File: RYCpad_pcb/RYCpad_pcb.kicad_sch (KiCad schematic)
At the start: 61 parts, among them J1 USB_C_Receptacle_USB2.0, J2 AVR ISP, K1 KEYSW, K10 KEYSW, K11 KEYSW, K12 KEYSW, K13 KEYSW, K14 KEYSW, K15 KEYSW, K16 KEYSW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

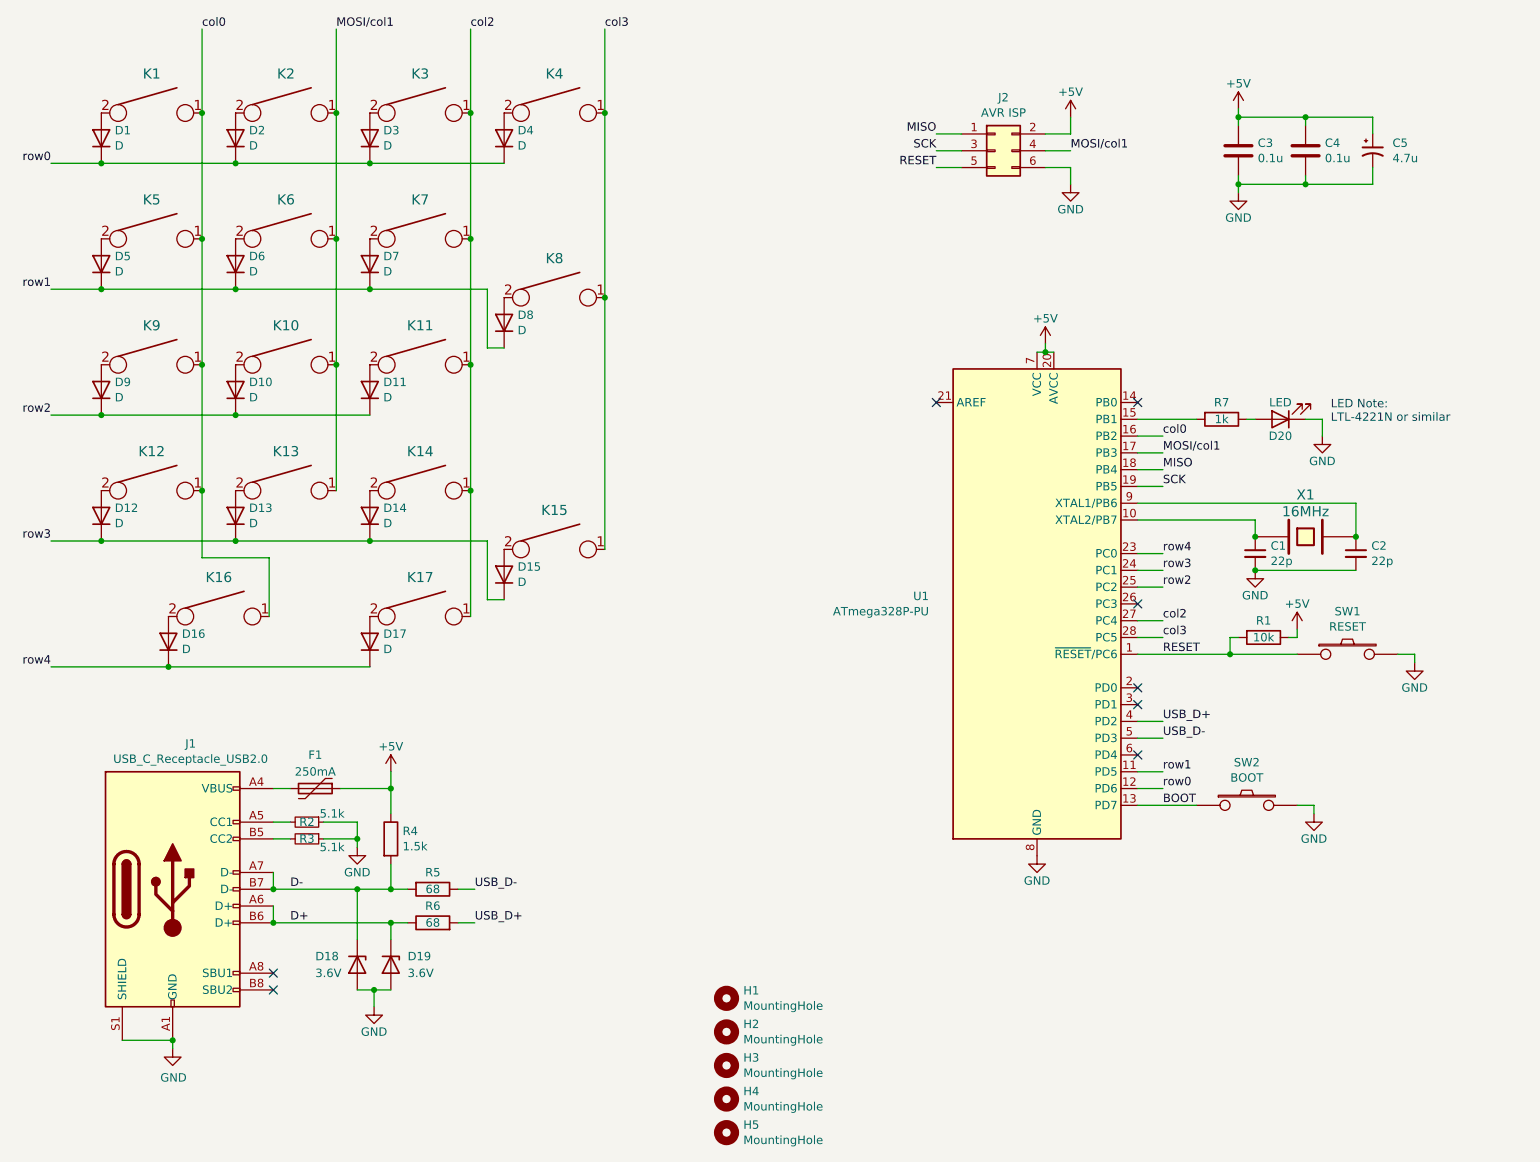
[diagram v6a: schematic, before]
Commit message: adjust col1 pin
change col1 pin PB3 >>> PC3
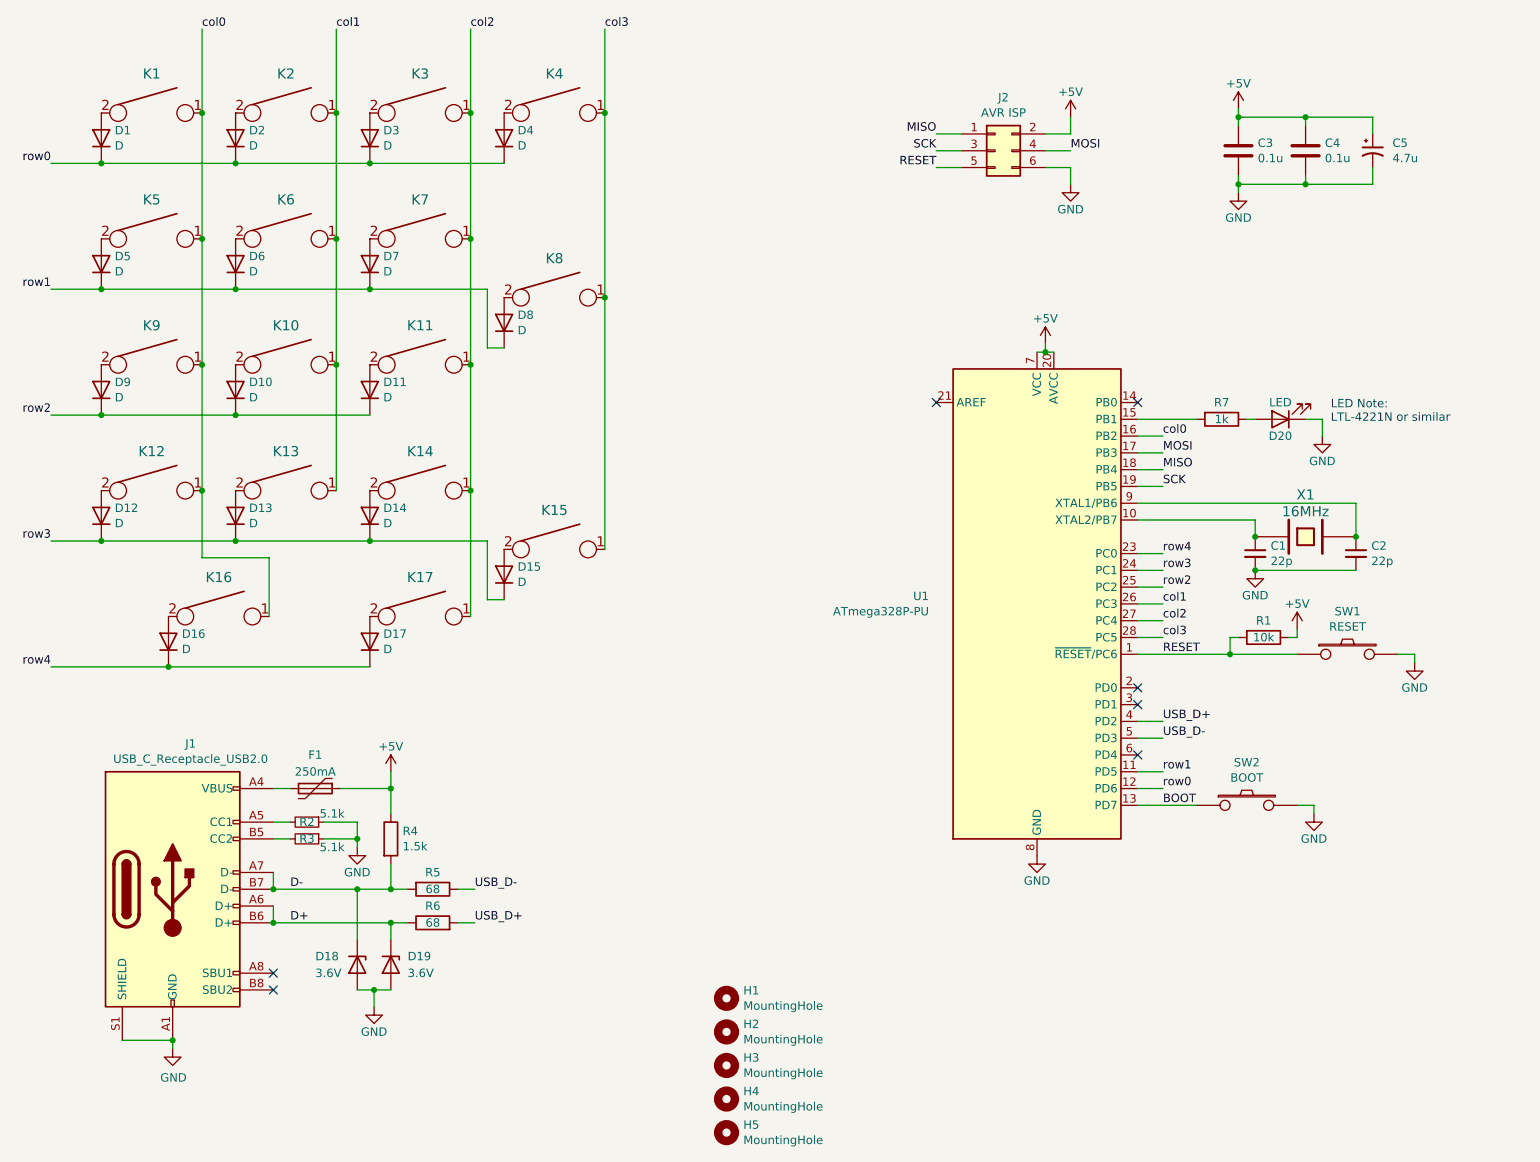
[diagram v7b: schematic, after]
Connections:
- net col1: now reaches U1.26 (PC3)
- net col1: now also K10.1, K13.1, K2.1, K6.1
- removed net MOSI/col1: J2.4 (Pin_4), K10.1, K13.1, K2.1, K6.1, U1.17 (PB3)
- new net MOSI: J2.4 (Pin_4), U1.17 (PB3)
- no-connect marks 8 -> 7
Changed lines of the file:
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@@
   (no_connect (at 217.17 124.46))
   (no_connect (at 86.36 170.18))
-  (no_connect (at 217.17 111.76))
   (no_connect (at 86.36 167.64))
   (no_connect (at 186.69 81.28))
@@
     (stroke (width 0) (type default) (color 0 0 0 0))
   )
+  (wire (pts (xy 217.17 111.76) (xy 220.98 111.76))
+    (stroke (width 0) (type default) (color 0 0 0 0))
+  )
   (wire (pts (xy 217.17 132.08) (xy 220.98 132.08))
     (stroke (width 0) (type default) (color 0 0 0 0))
@@
     (effects (font (size 1.27 1.27)) (justify left bottom))
   )
-  (label "MOSI{slash}col1" (at 95.885 24.765 0)
+  (label "col1" (at 95.885 24.765 0)
     (effects (font (size 1.27 1.27)) (justify left bottom))
   )
@@
     (effects (font (size 1.27 1.27)) (justify left bottom))
   )
-  (label "MOSI{slash}col1" (at 220.98 88.9 0)
+  (label "MOSI" (at 220.98 88.9 0)
     (effects (font (size 1.27 1.27)) (justify left bottom))
   )
@@
     (effects (font (size 1.27 1.27)) (justify left bottom))
   )
-  (label "MOSI{slash}col1" (at 207.01 43.18 0)
+  (label "MOSI" (at 207.01 43.18 0)
     (effects (font (size 1.27 1.27)) (justify left bottom))
   )
@@
     (effects (font (size 1.27 1.27)) (justify left bottom))
   )
+  (label "col1" (at 220.98 111.76 0)
+    (effects (font (size 1.27 1.27)) (justify left bottom))
+  )

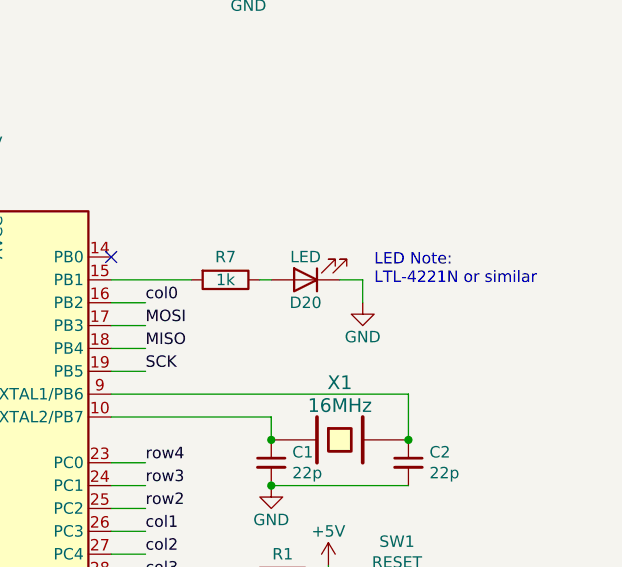
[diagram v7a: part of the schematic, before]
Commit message: change LED resistor default value
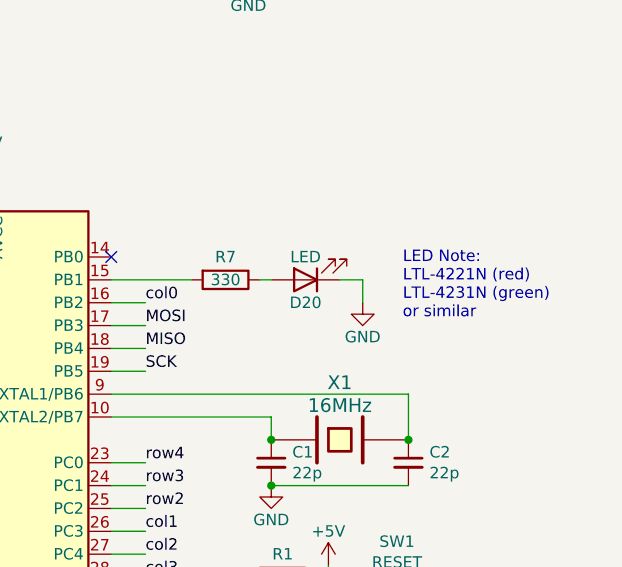
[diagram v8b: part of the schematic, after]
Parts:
- R7: value 1k -> 330
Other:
- note added: "LED Note: LTL-4221N (red) LTL-4231N (green) or similar"
- note removed: "LED Note: LTL-4221N or similar"
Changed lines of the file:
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@@
     (stroke (width 0) (type default) (color 0 0 0 0))
   )
-  (text "LED Note:\nLTL-4221N or similar" (at 246.38 84.455 0)
+  (text "LED Note:\nLTL-4221N (red)\nLTL-4231N (green)\nor similar"
+    (at 249.555 88.265 0)
     (effects (font (size 1.27 1.27)) (justify left bottom))
   )
@@
     (in_bom yes) (on_board yes)
     (property "Reference" "R7" (id 0) (at 229.87 81.28 90))
-    (property "Value" "1k" (id 1) (at 229.87 83.82 90))
+    (property "Value" "330" (id 1) (at 229.87 83.82 90))
     (property "Footprint" "Resistor_THT:R_Axial_DIN0204_L3.6mm_D1.6mm_P5.08mm_Horizontal" (id 2) (at 229.87 82.042 90)
       (effects (font (size 1.27 1.27)) hide)
@@
     )
     (path "/00000000-0000-0000-0000-000060876288"
-      (reference "R7") (unit 1) (value "1k") (footprint "Resistor_THT:R_Axial_DIN0204_L3.6mm_D1.6mm_P5.08mm_Horizontal")
+      (reference "R7") (unit 1) (value "330") (footprint "Resistor_THT:R_Axial_DIN0204_L3.6mm_D1.6mm_P5.08mm_Horizontal")
     )
     (path "/00000000-0000-0000-0000-0000608b5d4f"
